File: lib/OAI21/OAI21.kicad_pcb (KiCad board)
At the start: 2 copper layers, 6 parts

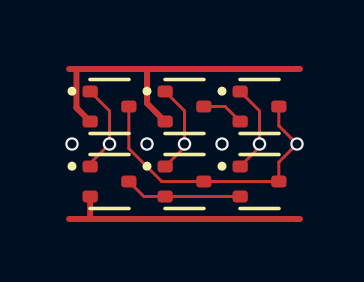
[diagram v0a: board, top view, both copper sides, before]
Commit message: High-density layout with pitch of 1.1mm, which gains 23% !!
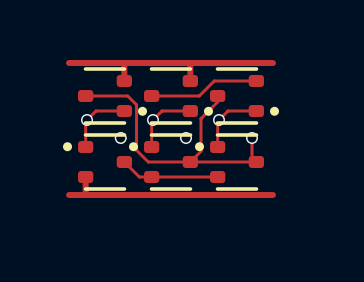
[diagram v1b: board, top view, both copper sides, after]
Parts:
- moved N3 0.99 mm to (5.50, 3.10)
- moved P3 0.83 mm to (5.50, 0.90), turned to 180 degrees
- moved N2 0.79 mm to (3.30, 3.10)
- moved N1 0.67 mm to (1.10, 3.10)
- moved P2 0.57 mm to (3.30, 0.90), turned to 180 degrees
- moved P1 0.38 mm to (1.10, 0.90), turned to 180 degrees
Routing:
- net VDD: track 11.6 -> 8.05 mm
- net intB: track 1.42 -> 3.70 mm
- net Y: track 9.86 -> 10.9 mm
- net GND: track 8.45 -> 7.41 mm
- net B2: track 3.03 -> 2.29 mm
- net B1: track 3.03 -> 2.29 mm
- net A: track 3.03 -> 2.29 mm
- net intN: track 3.92 -> 3.32 mm
- net (no net): vias 3 -> 2

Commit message: OAI21 layout was shifted up
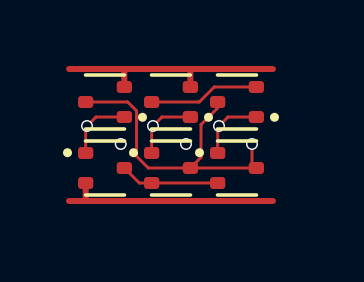
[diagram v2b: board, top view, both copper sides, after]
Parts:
- moved P1 0.20 mm to (1.10, 1.10)
- moved P2 0.20 mm to (3.30, 1.10)
- moved P3 0.20 mm to (5.50, 1.10)
- moved N1 0.20 mm to (1.10, 3.30)
- moved N2 0.20 mm to (3.30, 3.30)
- moved N3 0.20 mm to (5.50, 3.30)
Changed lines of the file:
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@@
 	(footprint "Package_TO_SOT_SMD:SOT-523"
 		(layer "F.Cu")
-		(at 1.1 0.9 180)
+		(at 1.1 1.1 180)
 		(descr "SOT523, https://www.diodes.com/assets/Package-Files/SOT523.pdf")
 		(tags "SOT-523")
@@
 	(footprint "Package_TO_SOT_SMD:SOT-523"
 		(layer "F.Cu")
-		(at 3.3 3.1)
+		(at 3.3 3.3)
 		(descr "SOT523, https://www.diodes.com/assets/Package-Files/SOT523.pdf")
 		(tags "SOT-523")
@@
 	(footprint "Package_TO_SOT_SMD:SOT-523"
 		(layer "F.Cu")
-		(at 3.3 0.9 180)
+		(at 3.3 1.1 180)
 		(descr "SOT523, https://www.diodes.com/assets/Package-Files/SOT523.pdf")
 		(tags "SOT-523")
@@
 	(footprint "Package_TO_SOT_SMD:SOT-523"
 		(layer "F.Cu")
-		(at 5.5 3.1)
+		(at 5.5 3.3)
 		(descr "SOT523, https://www.diodes.com/assets/Package-Files/SOT523.pdf")
 		(tags "SOT-523")
@@
 	(footprint "Package_TO_SOT_SMD:SOT-523"
 		(layer "F.Cu")
-		(at 5.5 0.9 180)
+		(at 5.5 1.1 180)
 		(descr "SOT523, https://www.diodes.com/assets/Package-Files/SOT523.pdf")
 		(tags "SOT-523")
@@
 	(footprint "Package_TO_SOT_SMD:SOT-523"
 		(layer "F.Cu")
-		(at 1.1 3.1)
+		(at 1.1 3.3)
 		(descr "SOT523, https://www.diodes.com/assets/Package-Files/SOT523.pdf")
 		(tags "SOT-523")
@@
 	)
 	(via
-		(at 1.625 2.3)
+		(at 1.625 2.5)
 		(size 0.4)
 		(drill 0.3)
@@
 	)
 	(via
-		(at 3.8 2.3)
+		(at 3.8 2.5)
 		(size 0.4)
 		(drill 0.3)
@@
 	)
 	(segment
-		(start 0.8 1.4)
-		(end 0.5 1.7)
+		(start 0.8 1.6)
+		(end 0.5 1.9)
 		(width 0.1)
 		(layer "F.Cu")
@@
 	)
 	(segment
-		(start 1.745 1.4)
-		(end 0.8 1.4)
+		(start 1.745 1.6)
+		(end 0.8 1.6)
 		(width 0.1)
 		(layer "F.Cu")
@@
 	)
 	(segment
-		(start 0.455 1.745)
-		(end 0.5 1.7)
+		(start 0.455 1.945)
+		(end 0.5 1.9)
 		(width 0.1)
 		(layer "F.Cu")
@@
 	)
 	(segment
-		(start 0.455 2.6)
-		(end 0.455 1.745)
+		(start 0.455 2.8)
+		(end 0.455 1.945)
 		(width 0.1)
 		(layer "F.Cu")
@@
 	)
 	(via
-		(at 0.5 1.7)
+		(at 0.5 1.9)
 		(size 0.4)
 		(drill 0.3)
@@
 	)
 	(segment
-		(start 0.455 3.6)
-		(end 0.455 4.175)
+		(start 0.455 3.8)
+		(end 0.455 4.375)
 		(width 0.2)
 		(layer "F.Cu")
@@
 	)
 	(segment
-		(start 0.48 4.2)
-		(end 6.7 4.2)
+		(start 0.48 4.4)
+		(end 6.7 4.4)
 		(width 0.2)
 		(layer "F.Cu")
@@
 	)
 	(segment
-		(start 0.455 4.175)
-		(end 0.48 4.2)
+		(start 0.455 4.375)
+		(end 0.48 4.4)
 		(width 0.2)
 		(layer "F.Cu")
@@
 	)
 	(segment
-		(start -0.1 4.2)
-		(end 0.48 4.2)
+		(start -0.1 4.4)
+		(end 0.48 4.4)
 		(width 0.2)
 		(layer "F.Cu")
@@
 	)
 	(segment
-		(start 3.945 3.1)
-		(end 2.542262 3.1)
+		(start 3.945 3.3)
+		(end 2.542262 3.3)
 		(width 0.1)
 		(layer "F.Cu")
@@
 	)
 	(segment
-		(start 1.857738 0.9)
-		(end 0.455 0.9)
+		(start 1.857738 1.1)
+		(end 0.455 1.1)
 		(width 0.1)
 		(layer "F.Cu")
@@
 	)
 	(segment
-		(start 4.855 0.9)
-		(end 4.855 1.099999)
+		(start 4.855 1.1)
+		(end 4.855 1.299999)
 		(width 0.1)
 		(layer "F.Cu")
@@
 	)
 	(segment
-		(start 4.3 2.745)
-		(end 3.945 3.1)
+		(start 4.3 2.945)
+		(end 3.945 3.3)
 		(width 0.1)
 		(layer "F.Cu")
@@
 	)
 	(segment
-		(start 6 2.955)
-		(end 6.145 3.1)
+		(start 6 3.155)
+		(end 6.145 3.3)
 		(width 0.1)
 		(layer "F.Cu")
@@
 	)
 	(segment
-		(start 4.3 1.654999)
-		(end 4.3 2.745)
+		(start 4.3 1.854999)
+		(end 4.3 2.945)
 		(width 0.1)
 		(layer "F.Cu")
@@
 	)
 	(segment
-		(start 2.151 1.193262)
-		(end 1.857738 0.9)
+		(start 2.151 1.393262)
+		(end 1.857738 1.1)
 		(width 0.1)
 		(layer "F.Cu")
@@
 	)
 	(segment
-		(start 4.855 1.099999)
-		(end 4.3 1.654999)
+		(start 4.855 1.299999)
+		(end 4.3 1.854999)
 		(width 0.1)
 		(layer "F.Cu")
@@
 	)
 	(segment
-		(start 6.145 3.1)
-		(end 3.945 3.1)
+		(start 6.145 3.3)
+		(end 3.945 3.3)
 		(width 0.1)
 		(layer "F.Cu")
@@
 	)
 	(segment
-		(start 6 2.3)
-		(end 6 2.955)
+		(start 6 2.5)
+		(end 6 3.155)
 		(width 0.1)
 		(layer "F.Cu")
@@
 	)
 	(segment
-		(start 2.151 2.708738)
-		(end 2.151 1.193262)
+		(start 2.151 2.908738)
+		(end 2.151 1.393262)
 		(width 0.1)
 		(layer "F.Cu")
@@
 	)
 	(segment
-		(start 2.542262 3.1)
-		(end 2.151 2.708738)
+		(start 2.542262 3.3)
+		(end 2.151 2.908738)
 		(width 0.1)
 		(layer "F.Cu")
@@
 	)
 	(via
-		(at 6 2.3)
+		(at 6 2.5)
 		(size 0.4)
 		(drill 0.3)
@@
 	)
 	(segment
-		(start 2.655 2.6)
-		(end 2.655 1.745)
+		(start 2.655 2.8)
+		(end 2.655 1.945)
 		(width 0.1)
 		(layer "F.Cu")
@@
 	)
 	(segment
-		(start 3 1.4)
-		(end 2.7 1.7)
+		(start 3 1.6)
+		(end 2.7 1.9)
 		(width 0.1)
 		(layer "F.Cu")
@@
 	)
 	(segment
-		(start 2.655 1.745)
-		(end 2.7 1.7)
+		(start 2.655 1.945)
+		(end 2.7 1.9)
 		(width 0.1)
 		(layer "F.Cu")
@@
 	)
 	(segment
-		(start 3.945 1.4)
-		(end 3 1.4)
+		(start 3.945 1.6)
+		(end 3 1.6)
 		(width 0.1)
 		(layer "F.Cu")
@@
 	)
 	(via
-		(at 2.7 1.7)
+		(at 2.7 1.9)
 		(size 0.4)
 		(drill 0.3)
@@
 	)
 	(segment
-		(start 4.742262 0.4)
-		(end 6.145 0.4)
+		(start 4.742262 0.6)
+		(end 6.145 0.6)
 		(width 0.1)
 		(layer "F.Cu")
@@
 	)
 	(segment
-		(start 2.655 0.9)
-		(end 4.242262 0.9)
+		(start 2.655 1.1)
+		(end 4.242262 1.1)
 		(width 0.1)
 		(layer "F.Cu")
@@
 	)
 	(segment
-		(start 4.242262 0.9)
-		(end 4.742262 0.4)
+		(start 4.242262 1.1)
+		(end 4.742262 0.6)
 		(width 0.1)
 		(layer "F.Cu")
@@
 	)
 	(segment
-		(start 5.2 1.4)
-		(end 4.9 1.7)
+		(start 5.2 1.6)
+		(end 4.9 1.9)
 		(width 0.1)
 		(layer "F.Cu")
@@
 	)
 	(segment
-		(start 6.145 1.4)
-		(end 5.2 1.4)
+		(start 6.145 1.6)
+		(end 5.2 1.6)
 		(width 0.1)
 		(layer "F.Cu")
@@
 	)
 	(segment
-		(start 4.855 1.745)
-		(end 4.9 1.7)
+		(start 4.855 1.945)
+		(end 4.9 1.9)
 		(width 0.1)
 		(layer "F.Cu")
@@
 	)
 	(segment
-		(start 4.855 2.6)
-		(end 4.855 1.745)
+		(start 4.855 2.8)
+		(end 4.855 1.945)
 		(width 0.1)
 		(layer "F.Cu")
@@
 	)
 	(via
-		(at 4.9 1.7)
+		(at 4.9 1.9)
 		(size 0.4)
 		(drill 0.3)
@@
 	)
 	(segment
-		(start 2.245 3.6)
-		(end 1.745 3.1)
+		(start 2.245 3.8)
+		(end 1.745 3.3)
 		(width 0.1)
 		(layer "F.Cu")
@@
 	)
 	(segment
-		(start 4.855 3.6)
-		(end 2.655 3.6)
+		(start 4.855 3.8)
+		(end 2.655 3.8)
 		(width 0.1)
 		(layer "F.Cu")
@@
 	)
 	(segment
-		(start 2.655 3.6)
-		(end 2.245 3.6)
+		(start 2.655 3.8)
+		(end 2.245 3.8)
 		(width 0.1)
 		(layer "F.Cu")
@@
 	)
 	(segment
-		(start 4 -0.2)
-		(end 6.7 -0.2)
+		(start 4 0)
+		(end 6.7 0)
 		(width 0.2)
 		(layer "F.Cu")
@@
 	)
 	(segment
-		(start 1.745 0.4)
-		(end 1.745 -0.145)
+		(start 1.745 0.6)
+		(end 1.745 0.055)
 		(width 0.2)
 		(layer "F.Cu")
@@
 	)
 	(segment
-		(start 1.745 -0.145)
-		(end 1.8 -0.2)
+		(start 1.745 0.055)
+		(end 1.8 0)
 		(width 0.2)
 		(layer "F.Cu")
@@
 	)
 	(segment
-		(start 3.945 0.4)
-		(end 3.945 -0.145)
+		(start 3.945 0.6)
+		(end 3.945 0.055)
 		(width 0.2)
 		(layer "F.Cu")
@@
 	)
 	(segment
-		(start -0.1 -0.2)
-		(end 1.8 -0.2)
+		(start -0.1 0)
+		(end 1.8 0)
 		(width 0.2)
 		(layer "F.Cu")
@@
 	)
 	(segment
-		(start 1.8 -0.2)
-		(end 4 -0.2)
+		(start 1.8 0)
+		(end 4 0)
 		(width 0.2)
 		(layer "F.Cu")
@@
 	)
 	(segment
-		(start 3.945 -0.145)
-		(end 4 -0.2)
+		(start 3.945 0.055)
+		(end 4 0)
 		(width 0.2)
 		(layer "F.Cu")

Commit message: All cells now use 1mm*4mm grid rather than 1.1mm*4.4mm
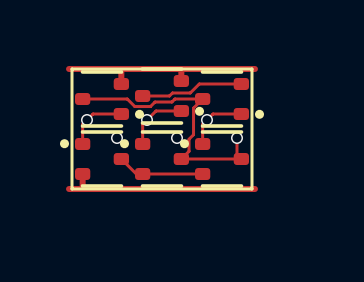
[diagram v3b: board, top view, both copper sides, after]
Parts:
- moved N3 0.58 mm to (5.00, 3.00)
- moved P3 0.51 mm to (5.00, 1.00)
- moved N2 0.42 mm to (3.00, 3.00)
- moved P2 0.36 mm to (3.00, 0.90)
- moved N1 0.32 mm to (1.00, 3.00)
- moved P1 0.14 mm to (1.00, 1.00)
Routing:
- net Y: track 10.9 -> 9.26 mm
- net VDD: track 8.05 -> 7.14 mm
- net GND: track 7.41 -> 6.72 mm

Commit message: Make the pads of my SOT523 footprint very slightly smaller, which is enough to route all the cells and leave the mosfets exactly on the grid
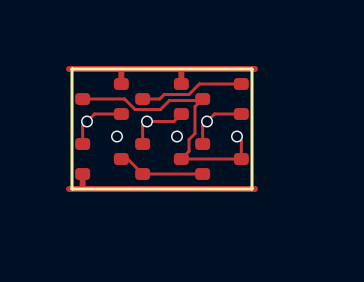
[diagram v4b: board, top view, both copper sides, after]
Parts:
- N1, N2, N3, P1, P2, P3: footprint Package_TO_SOT_SMD:SOT-523 -> RV523:SOT523
- moved P2 0.10 mm to (3.00, 1.00)

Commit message: Propagate MOSFET values to the cells' PCBs
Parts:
- N1, N2, N3: value (none) -> NMOS
- P1, P2, P3: value (none) -> PMOS
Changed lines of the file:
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@@
 			)
 		)
-		(property "Value" ""
+		(property "Value" "PMOS"
 			(at 0 0 180)
 			(layer "F.Fab")
@@
 			)
 		)
-		(property "Value" ""
+		(property "Value" "NMOS"
 			(at 0 0 0)
 			(layer "F.Fab")
@@
 			)
 		)
-		(property "Value" ""
+		(property "Value" "PMOS"
 			(at 0 0 180)
 			(layer "F.Fab")
@@
 			)
 		)
-		(property "Value" ""
+		(property "Value" "NMOS"
 			(at 0 0 0)
 			(layer "F.Fab")
@@
 			)
 		)
-		(property "Value" ""
+		(property "Value" "PMOS"
 			(at 0 0 180)
 			(layer "F.Fab")
@@
 			)
 		)
-		(property "Value" ""
-			(at 0 0 0)
-			(layer "F.Fab")
+		(property "Value" "NMOS"
+			(at 0 0 0)
+			(layer "F.Fab")
